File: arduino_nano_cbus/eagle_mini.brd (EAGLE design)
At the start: 100 x 80 mm, 28 parts, among them J1 1X2-3.5MM, J2 1X2-3.5MM, M1 ARDUINO-PRO-MINI-5.0V

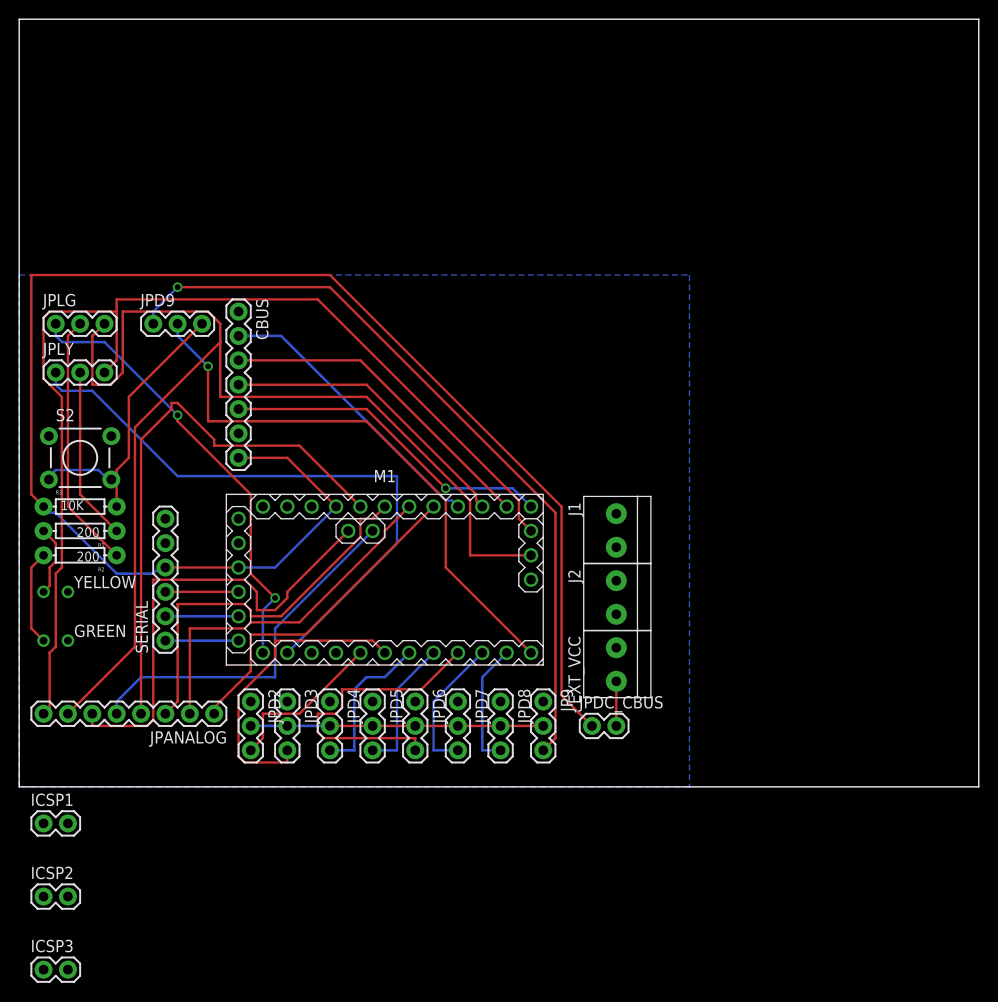
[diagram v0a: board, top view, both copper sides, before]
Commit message: car shield with atmega 328
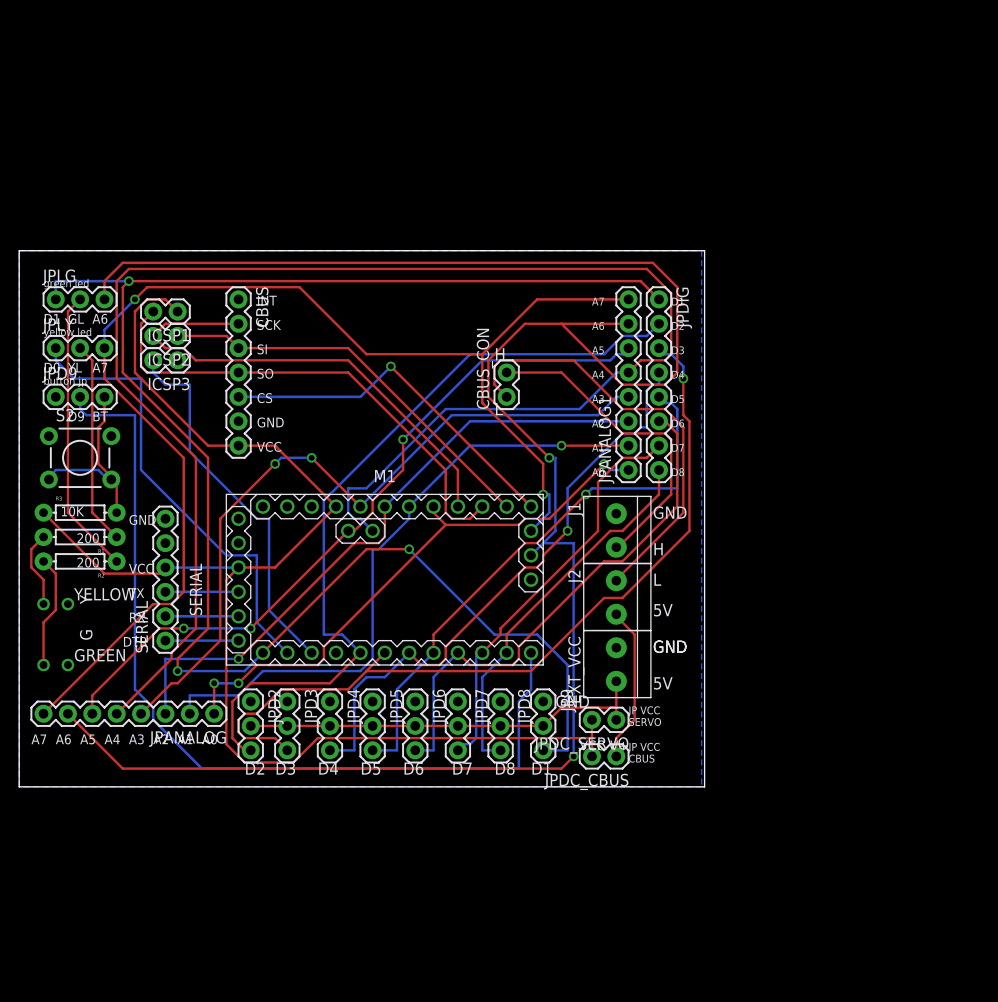
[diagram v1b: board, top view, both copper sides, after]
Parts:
- added CBUS_CON, JPDC_SERVO: M02PTH, SparkFun-Connectors:1X02
- added JPANALOG1, JPDIG: (no value), SparkFun-Connectors:1X08_ROUND
- moved ICSP3 65.0 mm to (16.5, 44.5), turned to 180 degrees
- moved ICSP2 60.1 mm to (16.5, 47.0), turned to 180 degrees
- moved ICSP1 55.1 mm to (16.5, 49.5), turned to 180 degrees
- moved JPD9 12.7 mm to (3.81, 40.6)
- moved JPDC_CBUS 4.07 mm to (62.2, 3.17), turned to 180 degrees
- moved GREEN 2.54 mm to (3.81, 12.7)
- moved JPLG 2.54 mm to (3.81, 50.8)
- moved JPLY 2.54 mm to (3.81, 45.7)
- moved YELLOW 1.27 mm to (3.81, 19.1)
- moved CBUS 1.27 mm to (22.9, 50.8)
- moved R1 0.64 mm to (6.35, 26.0)
- moved R3 0.64 mm to (6.35, 28.6)
- moved R2 0.63 mm to (6.35, 23.5)
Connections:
- removed net N$1: J2.2
- removed net N$15: J1.1
- removed net N$16: J1.2
- removed net N$3: J2.1
- removed net N$4: JP9.2, JPD2.2, JPD3.2, JPD4.2, JPD5.2, JPD6.2, JPD7.2, JPD8.2
- new net H: CBUS_CON.2, J1.2
- new net L: CBUS_CON.1, J2.1
- new net VBUS+: J2.2, JPDC_CBUS.1
- net A0: now also JPANALOG1.1
- net A1: now also JPANALOG1.2
- net A2: now also JPANALOG1.3
- net A3: now also JPANALOG1.4
- net A4: now also JPANALOG1.5
- net A5: now also JPANALOG1.6
- net A6: now also JPANALOG1.7
- net A7: now also JPANALOG1.8
- net D1: now also JP9.3, JPDIG.1
- net D2: now also JPDIG.2
- net D3: now also JPDIG.3
- net D4: now also JPDIG.4
- net D5: now also JPDIG.5
- net D6: now also JPDIG.6
- net D7: now also JPDIG.7
- net D8: now also JPDIG.8
- net GND: now also J1.1
- net JD9: no longer JP9.3
- net V+: now also JP9.2, JPD2.2, JPD3.2, JPD4.2, JPD5.2, JPD6.2, JPD7.2, JPD8.2, JPDC_SERVO.1; no longer JPDC_CBUS.2
- net VCC: now also JPDC_CBUS.2, JPDC_SERVO.2; no longer JPDC_CBUS.1
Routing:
- net D1: track 46.9 -> 173.8 mm, vias 2 -> 3
- net A4: track 38.3 -> 162.9 mm
- net A6: track 123.1 -> 209.4 mm, vias 0 -> 2
- net JD9: track 79.3 -> 0.00 mm, vias 1 -> 0
- net D2: track 17.1 -> 82.8 mm
- net D3: track 32.2 -> 85.7 mm, vias 0 -> 1
- net D4: track 16.2 -> 62.1 mm, vias 0 -> 1
- net L: track 0.00 -> 45.4 mm
- net D5: track 14.3 -> 58.6 mm, vias 0 -> 1
- net RST: track 0.00 -> 39.6 mm
- net V+: track 4.65 -> 42.9 mm
- net H: track 0.00 -> 34.0 mm
- net D9: track 59.2 -> 92.6 mm, vias 1 -> 0
- net N$4: track 30.5 -> 0.00 mm
- net A1: track 37.4 -> 65.8 mm, vias 0 -> 1
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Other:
- board size 100 x 80 mm -> 71.4 x 55.9 mm
- board text added: "5V"
- board text added: "A0"
- board text added: "A1"
- board text added: "A2"
- board text added: "A3"
- board text added: "A4"
- board text added: "A5"
- board text added: "A6"
- board text added: "A7"
- board text added: "BT"
- board text added: "CS"
- board text added: "D0"
- board text added: "D1"
- board text added: "D2"
- board text added: "D3"
- board text added: "D4"
- board text added: "D5"
- board text added: "D6"
- board text added: "D7"
- board text added: "D8"
- board text added: "D9"
- board text added: "DTR"
- board text added: "G"
- board text added: "GL"
- board text added: "GND"
- board text added: "H"
- board text added: "INT"
- board text added: "JP VCC CBUS"
- board text added: "JP VCC SERVO"
- board text added: "L"
- board text added: "RX"
- board text added: "SCK"
- board text added: "SERIAL"
- board text added: "SI"
- board text added: "SO"
- board text added: "TX"
- board text added: "V+"
- board text added: "VCC"
- board text added: "Y"
- board text added: "YL"
- board text added: "button jp"
- board text added: "green led"
- board text added: "yellow led"

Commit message: some improvement on the boards.
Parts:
- added C1, C2: 100uF, adafruit:E2,5-6
- moved EXT_VCC 7.62 mm to (69.8, 12.7)
- moved J1 7.62 mm to (69.8, 26.7)
- moved J2 7.62 mm to (69.8, 19.7)
- moved JPDC_CBUS 7.62 mm to (69.8, 3.17)
- moved JPDC_SERVO 7.62 mm to (69.8, 6.99)
- moved JPDIG 6.98 mm to (73.7, 50.8)
- moved JPANALOG1 6.35 mm to (69.8, 33.0)
- moved CBUS 3.81 mm to (22.9, 54.6)
- moved CBUS_CON 3.81 mm to (50.8, 44.5)
- moved ICSP1 3.81 mm to (16.5, 53.3)
- moved ICSP2 3.81 mm to (16.5, 50.8)
- moved ICSP3 3.81 mm to (16.5, 48.3)
- moved JPLG 2.54 mm to (3.81, 53.3)
- moved JP9 2.54 mm to (57.1, 8.89)
- moved JPD3 2.54 mm to (30.5, 8.89)
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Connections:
- net GND: now also C1.-, C2.-
- net VCC: now also C1.+, C2.+
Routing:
- net A4: track 162.9 -> 94.0 mm, vias 0 -> 2
- net A2: track 66.1 -> 85.8 mm, vias 1 -> 2
- net D6: track 54.1 -> 73.8 mm
- net D8: track 39.5 -> 58.0 mm
- net D7: track 42.7 -> 61.0 mm
- net D9: track 92.6 -> 74.7 mm, vias 0 -> 1
- net A5: track 75.4 -> 89.7 mm
- net A6: track 209.4 -> 221.8 mm, vias 2 -> 0
- net A7: track 134.8 -> 145.7 mm, vias 2 -> 3
- net D2: track 82.8 -> 92.7 mm, vias 0 -> 1
- net A3: track 76.1 -> 85.8 mm
- net L: track 45.4 -> 36.0 mm
- net A1: track 65.8 -> 74.1 mm, vias 1 -> 2
- net D4: track 62.1 -> 70.3 mm, vias 1 -> 4
- net V+: track 42.9 -> 50.5 mm
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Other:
- board size 71.4 x 55.9 mm -> 77.8 x 58.4 mm

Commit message: bug fixes and better board routing
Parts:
- moved CBUS_CON 4.58 mm to (54.6, 47.0)
- moved CBUS 4.02 mm to (26.7, 55.9)
- moved C2 2.84 mm to (16.5, 44.5)
- moved ICSP2 2.54 mm to (16.5, 53.3)
- moved ICSP1 2.54 mm to (16.5, 55.9)
- moved ICSP3 2.54 mm to (16.5, 50.8)
- moved M1 2.54 mm to (40.6, 21.6)
- moved C1 1.80 mm to (16.5, 35.6)
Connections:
- net A0: now also JPLG.3
- net A1: now also JPLY.3
- net A6: no longer JPLG.3
- net A7: no longer JPLY.3
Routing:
- net GND: track 0.00 -> 193.6 mm
- net A6: track 221.8 -> 106.3 mm, vias 0 -> 1
- net A0: track 63.0 -> 139.9 mm, vias 1 -> 0
- net A1: track 74.1 -> 132.5 mm, vias 2 -> 0
- net VCC: track 130.9 -> 179.8 mm
- net A2: track 85.8 -> 122.9 mm, vias 2 -> 1
- net D5: track 55.9 -> 87.9 mm, vias 2 -> 0
- net A7: track 145.7 -> 116.4 mm, vias 3 -> 1
- net D4: track 70.3 -> 97.9 mm, vias 4 -> 0
- net H: track 35.6 -> 51.3 mm
- net SI: track 43.2 -> 58.0 mm, vias 0 -> 1
- net RST: track 41.1 -> 54.4 mm, vias 0 -> 1
- net SO: track 50.2 -> 62.7 mm, vias 0 -> 1
- net D3: track 85.3 -> 96.4 mm, vias 1 -> 0
- net SCK: track 46.5 -> 57.6 mm
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- removed copper zone on layer 16, net GND
